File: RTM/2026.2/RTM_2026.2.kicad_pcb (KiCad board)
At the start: 2 copper layers, 71 x 54.8 mm, 45 parts, among them J1 V_BIAS TEST, J2 Conn_01x02, J3 12V TEST, J4 V_IN TEST, J5 Conn_01x02, J7 Conn_01x02, Q2 NMOS, Q4 NMOS, Q5 NMOS, U1 MMSZ5245BT1G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

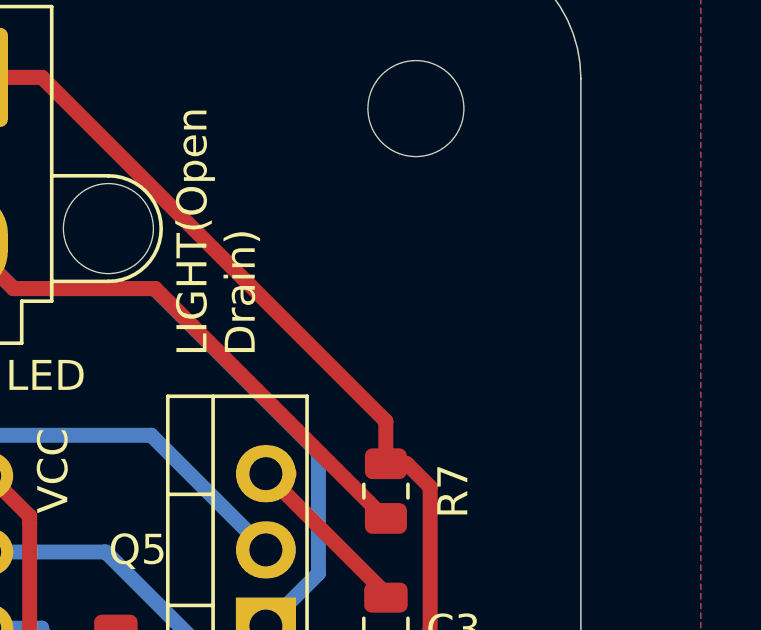
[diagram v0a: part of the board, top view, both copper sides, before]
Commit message: Added logo to front silkscreen
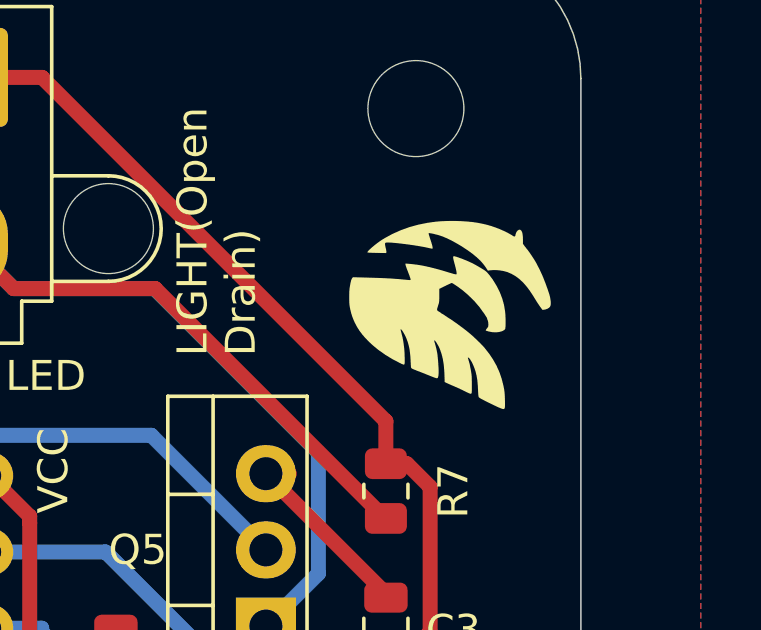
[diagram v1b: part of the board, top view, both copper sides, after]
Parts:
- added G***: LOGO, EVRacingLogoLibraryKiCad:EVRacingOnlyLogo, F.Cu at (87.0, 34.5)

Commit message: Updated silkscreen based on Gabe's revisions #2
Fixed missing resistor (R15) on layout
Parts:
- added R15: 20k, Resistor_SMD:R_0805_2012Metric, F.Cu at (46.0, 27.0)
- moved R13 3.55 mm to (50.9, 29.0)
- moved R14 2.33 mm to (50.0, 25.0)
- renumbered HV_DETECTED_LED to DEBUG_1, FLOATING_PWR_LED to DEBUG_2, GLV_PWR_LED to DEBUG_3
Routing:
- net V_IN: track 20.7 -> 23.7 mm
- net Net-(R13-Pad2): track 1.95 -> 4.38 mm
- net Net-(R14-Pad1): track 1.92 -> 3.00 mm
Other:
- board text added: "HIGH VOLTAGE"
- board text added: "ISOLATED ZONE"
- board text added: "LOW VOLTAGE"
- board text added: "LV +12V"
- board text removed: "+12V ISO"
- board text removed: "ISOLATED"
- board text removed: "NON-ISOLATED"

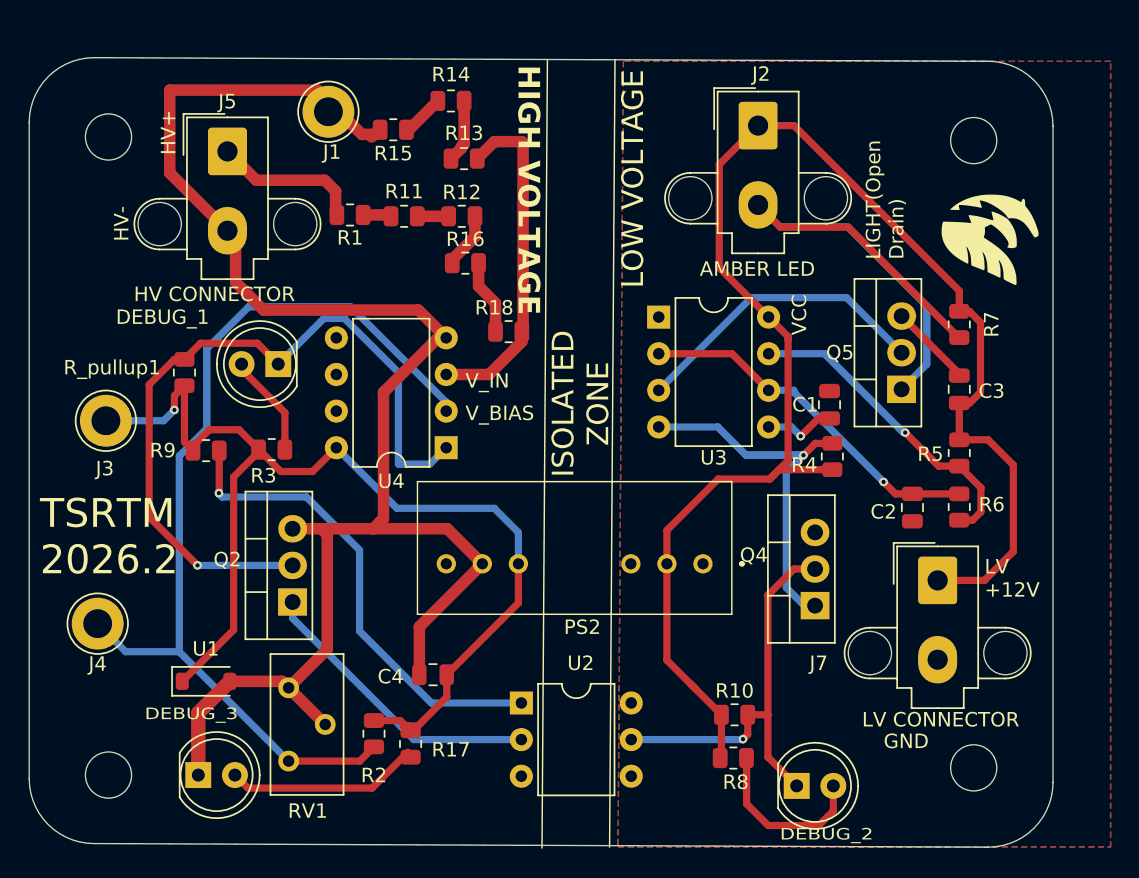
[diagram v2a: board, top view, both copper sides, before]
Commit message: Changed all NMOS to GDS
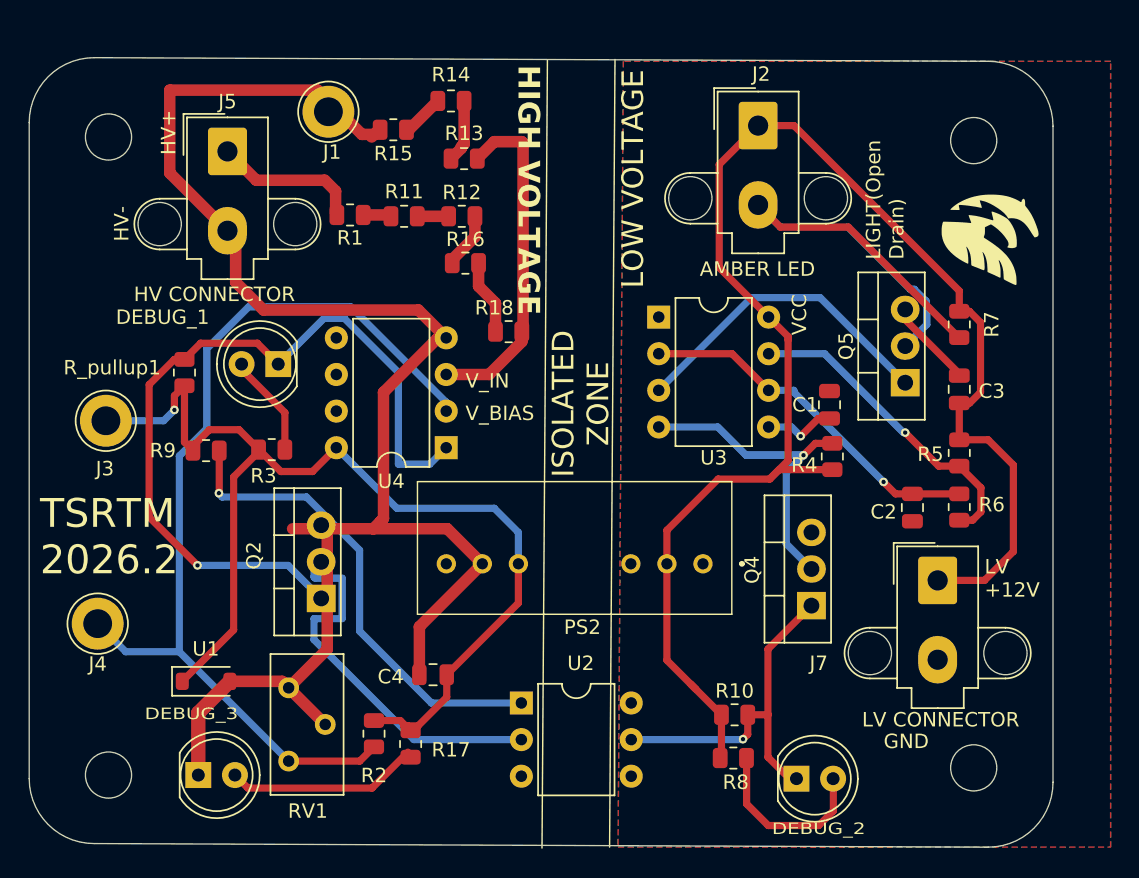
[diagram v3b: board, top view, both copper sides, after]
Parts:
- moved Q2 2.00 mm to (41.0, 59.5)
- moved Q5 0.52 mm to (81.5, 44.5)
- moved DEBUG_2 0.50 mm to (74.0, 72.0)
- moved Q4 0.25 mm to (75.0, 60.0)
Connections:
- Q2 pad 1: Net-(Q2-D) -> Net-(DEBUG_1-K)
- Q2 pad 2: Net-(DEBUG_1-K) -> Net-(Q2-D)
- Q4 pad 1: Net-(Q4-D) -> Net-(DEBUG_2-K)
- Q4 pad 2: Net-(DEBUG_2-K) -> Net-(Q4-D)
- Q5 pad 1: Net-(J2-Pin_2) -> Net-(Q5-G)
- Q5 pad 2: Net-(Q5-G) -> Net-(J2-Pin_2)
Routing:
- net Net-(Q2-D): track 20.5 -> 26.7 mm
- net Net-(Q4-D): track 29.3 -> 26.2 mm
- net Net-(J2-Pin_2): track 38.9 -> 35.9 mm
- net Net-(DEBUG_1-K): track 52.6 -> 55.5 mm
- net Net-(DEBUG_2-K): track 29.2 -> 26.5 mm
- net Net-(Q5-G): track 21.1 -> 22.2 mm

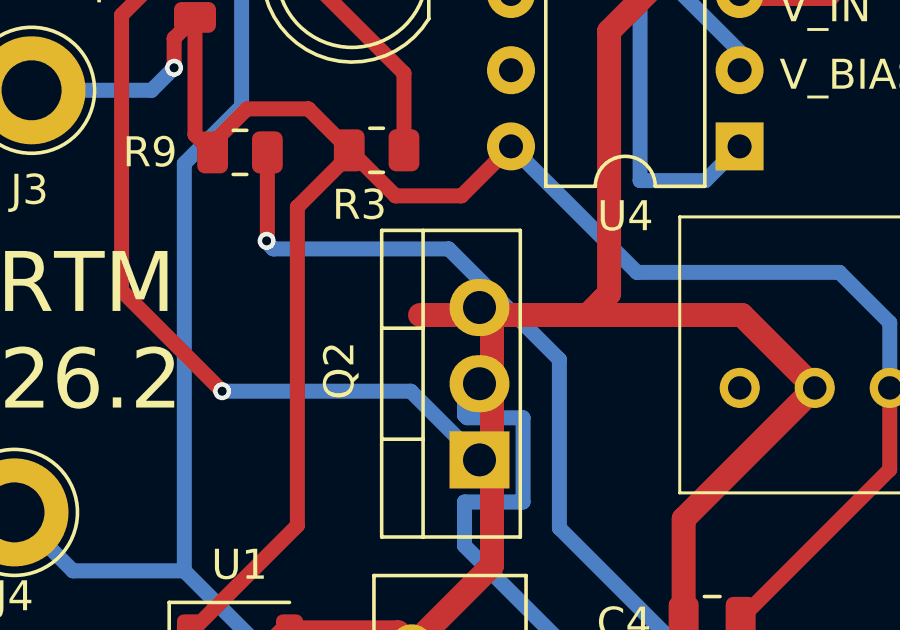
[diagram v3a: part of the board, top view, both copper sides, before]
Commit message: Deleted extra trace
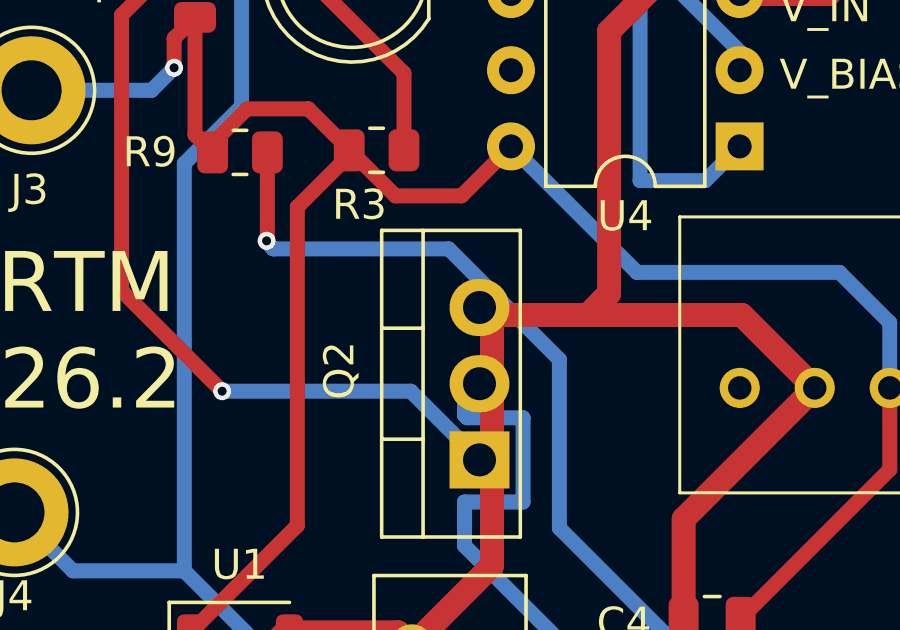
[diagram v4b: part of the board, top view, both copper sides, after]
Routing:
- net HighVoltage-: track 114.7 -> 112.7 mm
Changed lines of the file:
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@@
-	)
-	(segment
-		(start 39.016847 54.67)
-		(end 41.016847 54.67)
-		(width 0.8)
-		(layer "F.Cu")
-		(net 2)
 	)
 	(segment
